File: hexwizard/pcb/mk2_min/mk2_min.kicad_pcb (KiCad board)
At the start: 2 copper layers, 53 x 99.5 mm, 23 parts, among them J1 SN-U110 card edge, J2 OLED I2C, J4 USB-C, Q1 2N7002, Q2 2N7002 (AO3400 if it droops), SW1 BOOT / USER, U1 SST39SF040-70-4C-TU, U2 ESP32-S3-WROOM-1-N16, U3 AP2112K-3.3

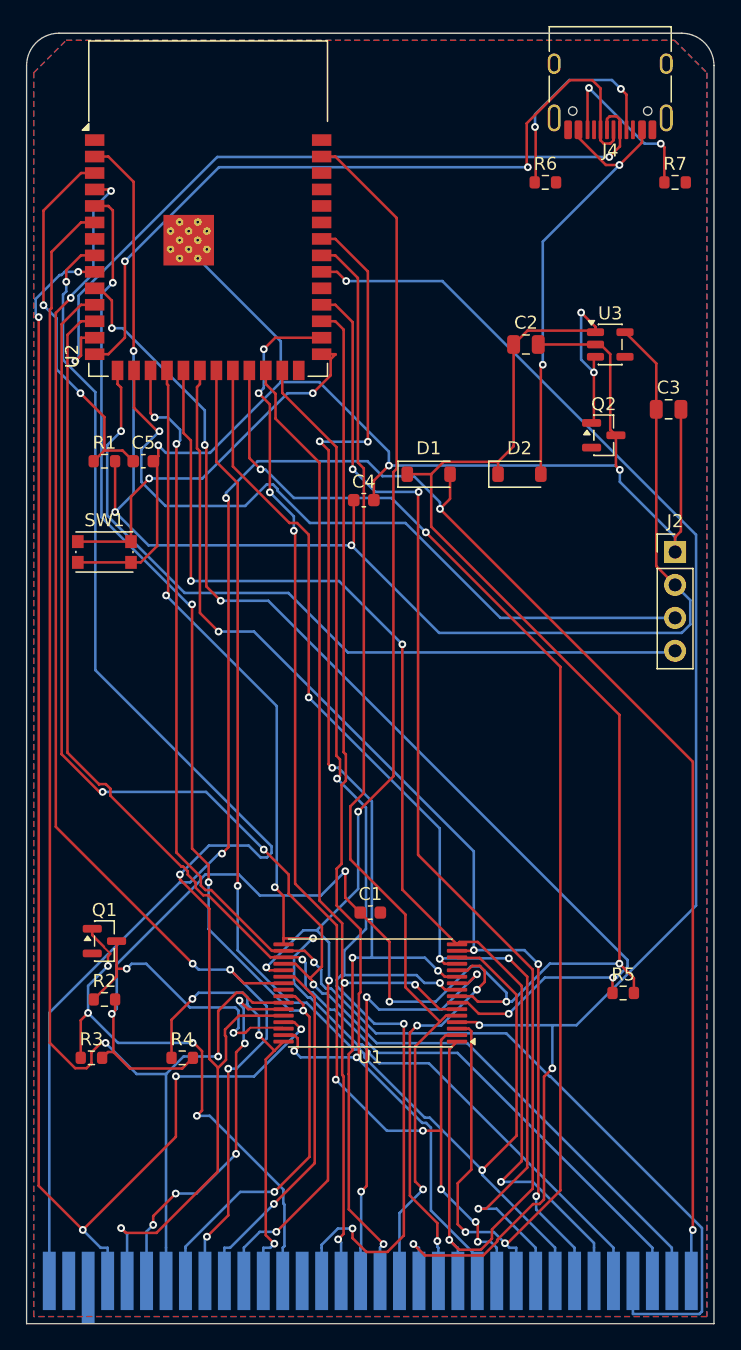
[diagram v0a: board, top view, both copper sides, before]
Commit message: hexwizard: proposed MK2 prototype, mk2_min fully routed (untested), BOM and README
mk2_min is now fully autorouted (0 unconnected, no clearance errors in DRC) with a
refreshed BOM, parts table and GPIO map. Still unbuilt and untested.

Co-Authored-By: Claude Sonnet 5.5 <noreply@anthropic.com>
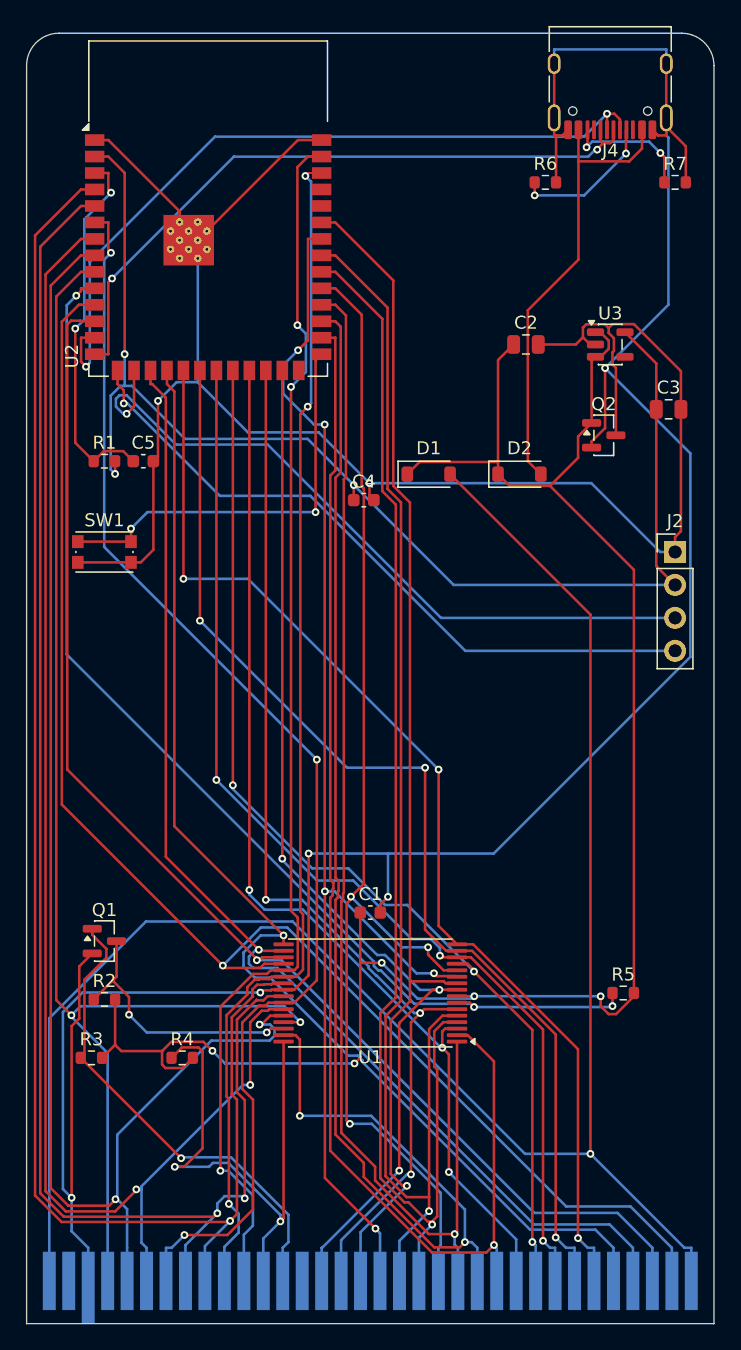
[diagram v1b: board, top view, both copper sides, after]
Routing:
- net GND: track 0.00 -> 197.4 mm, vias 0 -> 5
- net D5: track 29.6 -> 111.3 mm, vias 5 -> 2
- net D1: track 28.1 -> 92.2 mm, vias 1 -> 3
- net A12: track 30.7 -> 94.0 mm
- net A16: track 33.9 -> 91.5 mm, vias 3 -> 1
- net ESP_GND: track 117.2 -> 145.2 mm, vias 3 -> 2
- net A8: track 108.1 -> 83.0 mm, vias 4 -> 3
- net D3: track 99.6 -> 120.8 mm, vias 5 -> 2
- net D2: track 102.2 -> 123.0 mm, vias 6 -> 1
- net A10: track 87.9 -> 107.9 mm
- net A6: track 102.7 -> 85.1 mm, vias 2 -> 3
- net A13: track 117.3 -> 100.7 mm, vias 4 -> 1
- net SLOT_5V: track 157.1 -> 142.7 mm, vias 4 -> 1
- net V5: track 158.7 -> 144.4 mm, vias 7 -> 5
- net A14: track 87.6 -> 101.6 mm
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- removed copper zone on B.Cu, net GND
- removed copper zone on F.Cu, net GND
